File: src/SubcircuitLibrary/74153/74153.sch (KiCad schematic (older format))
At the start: 15 parts, among them U1 PORT, U2 d_inverter, U3 d_inverter, U34 d_inverter, U35 d_inverter, X1 4_OR, X10 4_and, X2 4_OR, X3 4_and, X4 4_and, X5 4_and, X6 4_and, X7 4_and, X8 4_and, X9 4_and

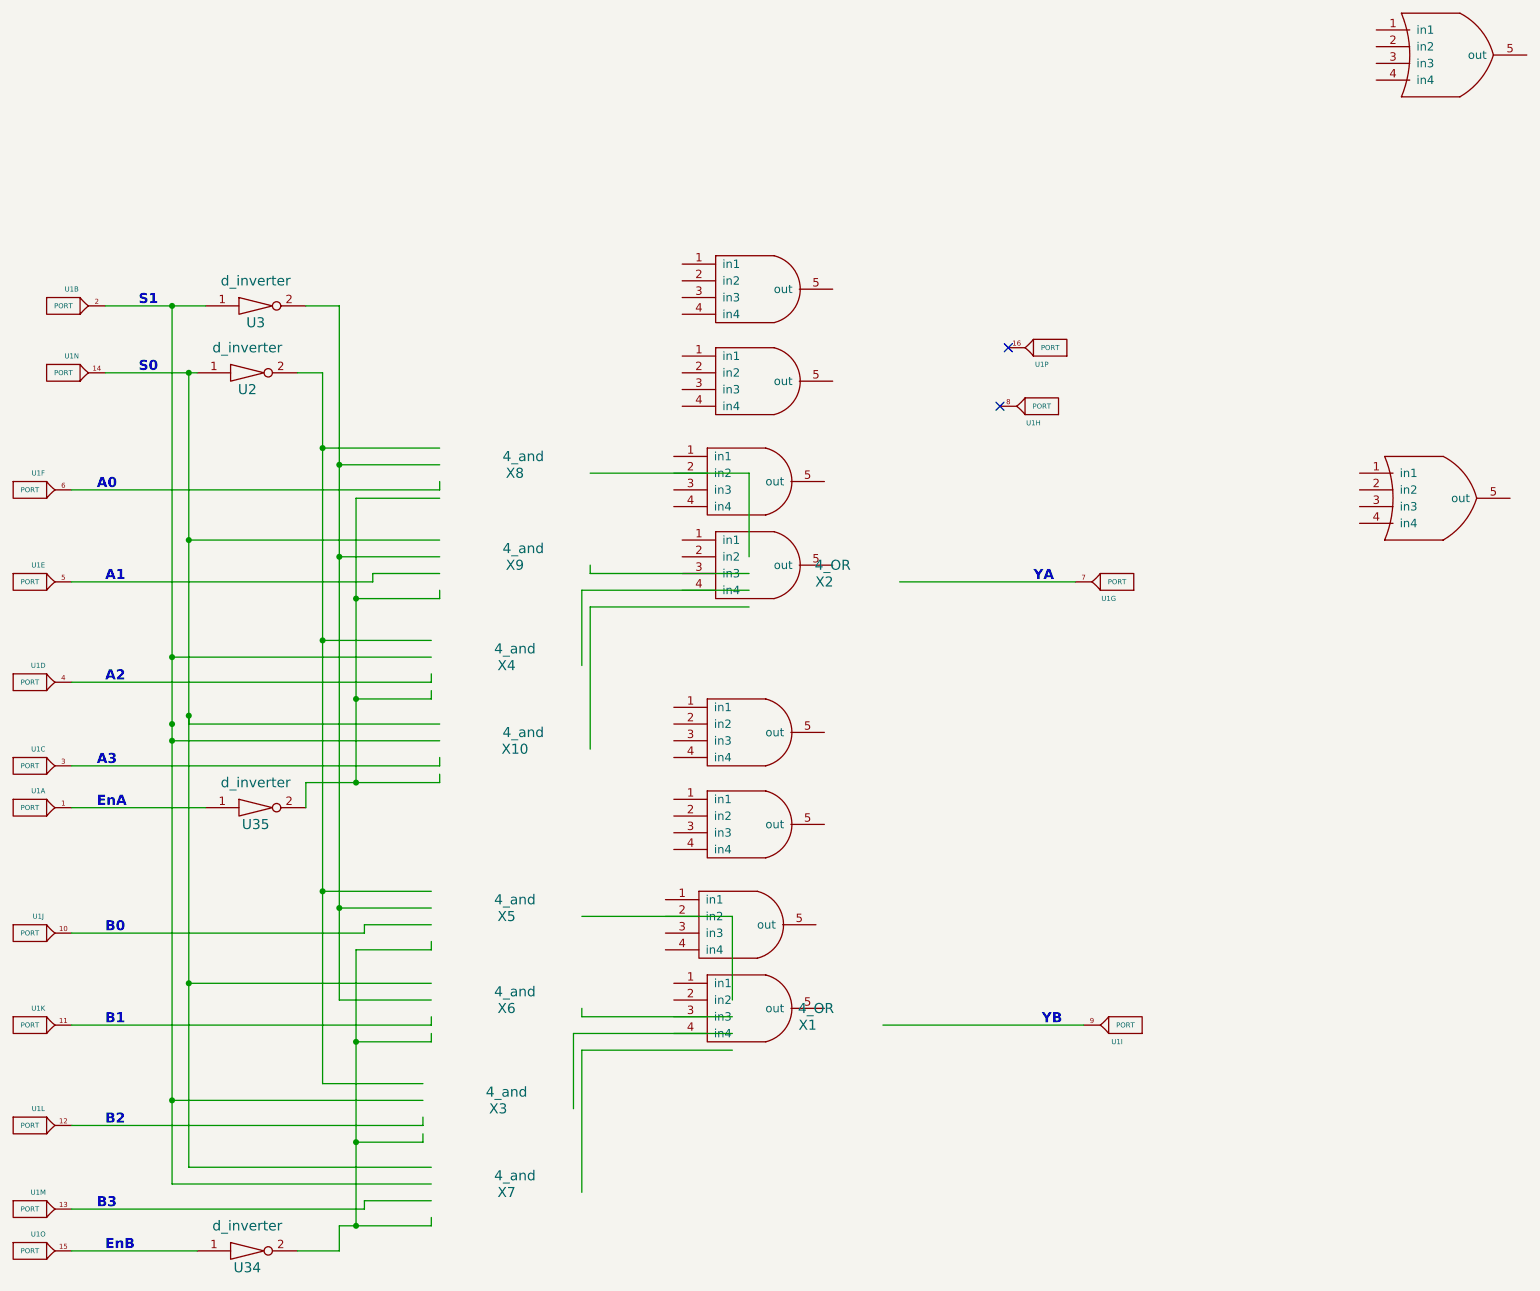
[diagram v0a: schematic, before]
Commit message: common code for Win and Linux, merged py2 changes
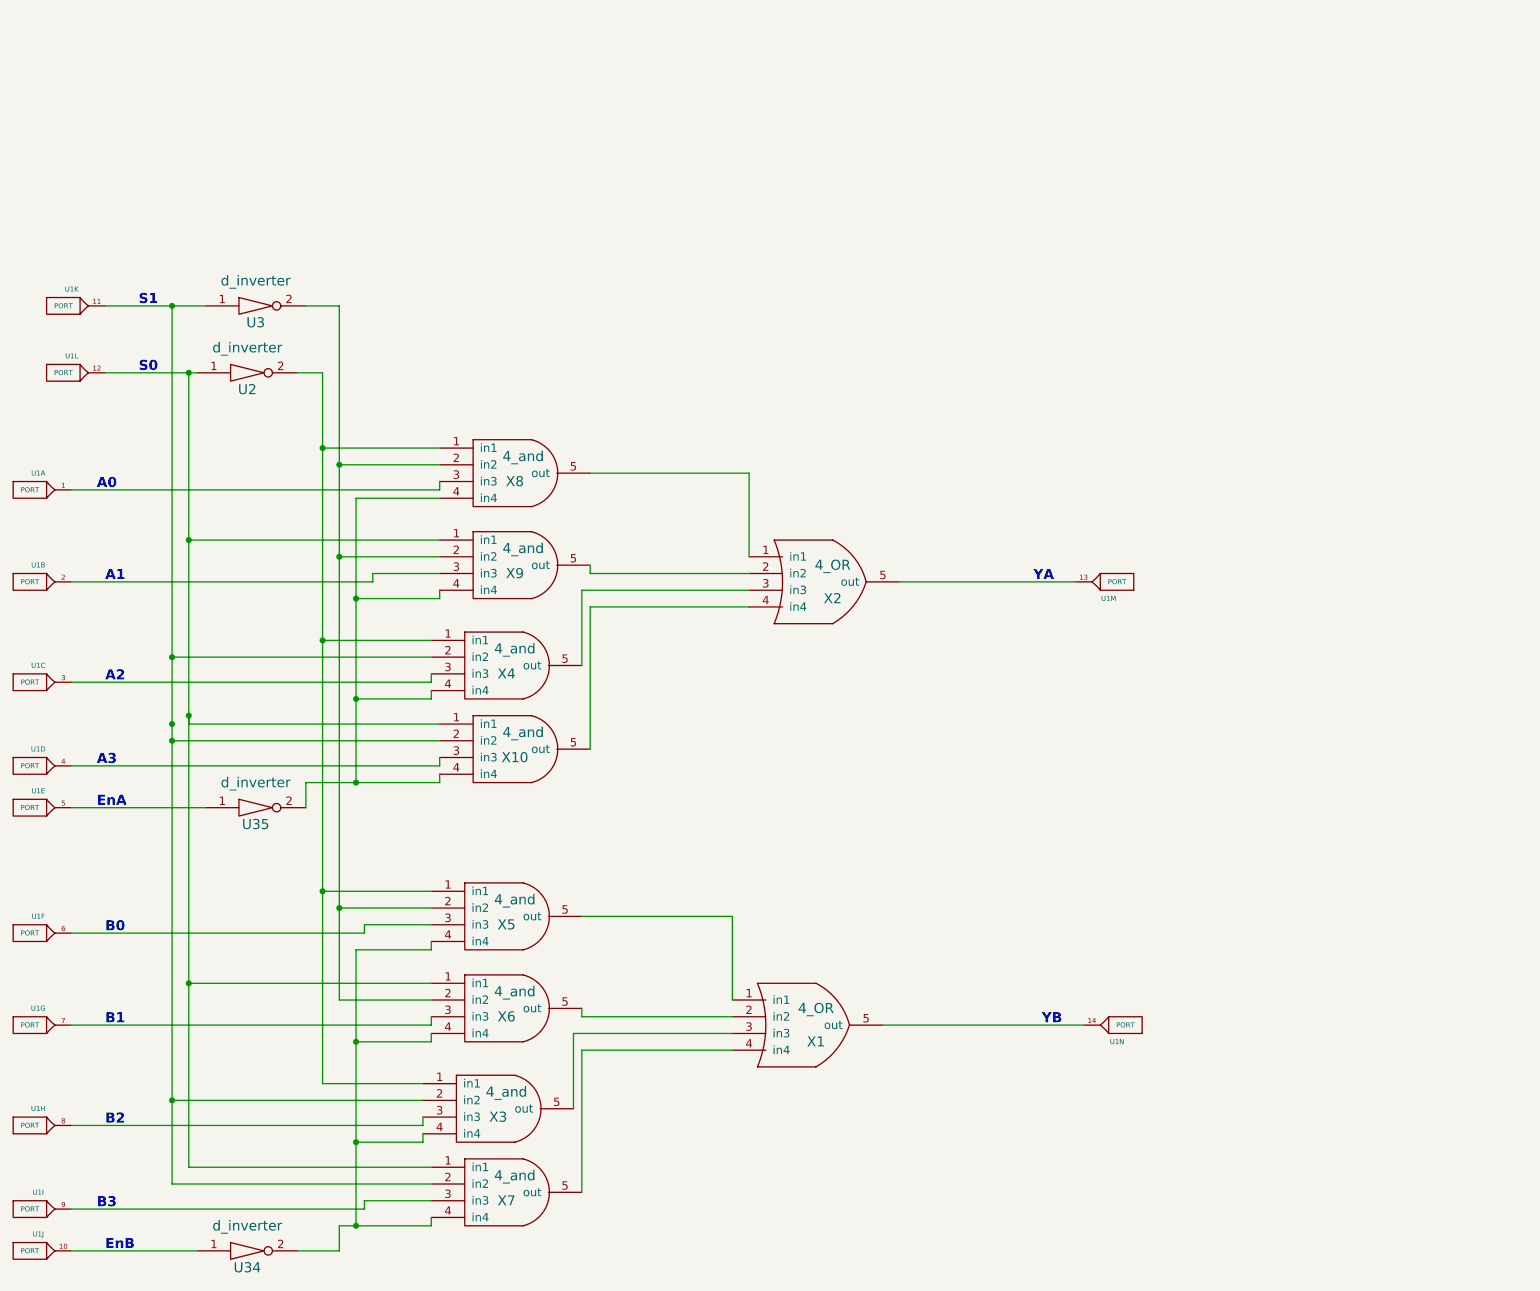
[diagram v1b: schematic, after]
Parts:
- removed unit 16 of U1
- removed unit 8 of U1
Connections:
- no-connect marks 2 -> 0
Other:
- moved on the sheet: X1, X10, X2, X3, X4, X5, X6, X7, X8, X9
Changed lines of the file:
@@
 EESchema Schematic File Version 2
+LIBS:power
+LIBS:device
+LIBS:texas
+LIBS:intel
+LIBS:audio
+LIBS:interface
+LIBS:digital-audio
+LIBS:philips
+LIBS:display
+LIBS:cypress
+LIBS:siliconi
+LIBS:opto
+LIBS:atmel
+LIBS:contrib
+LIBS:valves
 LIBS:eSim_Analog
 LIBS:eSim_Devices
@@
 LIBS:eSim_Plot
 LIBS:eSim_Power
+LIBS:eSim_PSpice
 LIBS:eSim_Sources
+LIBS:eSim_User
 LIBS:eSim_Subckt
-LIBS:eSim_User
 LIBS:74153-cache
 EELAYER 25 0
@@
 $Comp
 L PORT U1
-U 6 1 5C93A0F9
+U 1 1 5C93A0F9
 P 1350 2050
 F 0 "U1" H 1400 2150 30  0000 C CNN
@@
 F 2 "" H 1350 2050 60  0000 C CNN
 F 3 "" H 1350 2050 60  0000 C CNN
-	6    1350 2050
-	1    0    0    -1
-$EndComp
-$Comp
-L PORT U1
-U 10 1 5C93A174
+	1    1350 2050
+	1    0    0    -1
+$EndComp
+$Comp
+L PORT U1
+U 6 1 5C93A174
 P 1350 4700
 F 0 "U1" H 1400 4800 30  0000 C CNN
@@
 F 2 "" H 1350 4700 60  0000 C CNN
 F 3 "" H 1350 4700 60  0000 C CNN
-	10   1350 4700
-	1    0    0    -1
-$EndComp
-$Comp
-L PORT U1
-U 5 1 5C93AA3C
+	6    1350 4700
+	1    0    0    -1
+$EndComp
+$Comp
+L PORT U1
+U 2 1 5C93AA3C
 P 1350 2600
 F 0 "U1" H 1400 2700 30  0000 C CNN
@@
 F 2 "" H 1350 2600 60  0000 C CNN
 F 3 "" H 1350 2600 60  0000 C CNN
-	5    1350 2600
-	1    0    0    -1
-$EndComp
-$Comp
-L PORT U1
-U 4 1 5C93AACB
+	2    1350 2600
+	1    0    0    -1
+$EndComp
+$Comp
+L PORT U1
+U 3 1 5C93AACB
 P 1350 3200
 F 0 "U1" H 1400 3300 30  0000 C CNN
@@
 F 2 "" H 1350 3200 60  0000 C CNN
 F 3 "" H 1350 3200 60  0000 C CNN
-	4    1350 3200
-	1    0    0    -1
-$EndComp
-$Comp
-L PORT U1
-U 3 1 5C93AB5F
+	3    1350 3200
+	1    0    0    -1
+$EndComp
+$Comp
+L PORT U1
+U 4 1 5C93AB5F
 P 1350 3700
 F 0 "U1" H 1400 3800 30  0000 C CNN
@@
 F 2 "" H 1350 3700 60  0000 C CNN
 F 3 "" H 1350 3700 60  0000 C CNN
-	3    1350 3700
-	1    0    0    -1
-$EndComp
-$Comp
-L PORT U1
-U 11 1 5C93AD97
+	4    1350 3700
+	1    0    0    -1
+$EndComp
+$Comp
+L PORT U1
+U 7 1 5C93AD97
 P 1350 5250
 F 0 "U1" H 1400 5350 30  0000 C CNN
@@
 F 2 "" H 1350 5250 60  0000 C CNN
 F 3 "" H 1350 5250 60  0000 C CNN
-	11   1350 5250
-	1    0    0    -1
-$EndComp
-$Comp
-L PORT U1
-U 12 1 5C93ADFC
+	7    1350 5250
+	1    0    0    -1
+$EndComp
+$Comp
+L PORT U1
+U 8 1 5C93ADFC
 P 1350 5850
 F 0 "U1" H 1400 5950 30  0000 C CNN
@@
 F 2 "" H 1350 5850 60  0000 C CNN
 F 3 "" H 1350 5850 60  0000 C CNN
-	12   1350 5850
-	1    0    0    -1
-$EndComp
-$Comp
-L PORT U1
-U 13 1 5C93AE63
+	8    1350 5850
+	1    0    0    -1
+$EndComp
+$Comp
+L PORT U1
+U 9 1 5C93AE63
 P 1350 6350
 F 0 "U1" H 1400 6450 30  0000 C CNN
@@
 F 2 "" H 1350 6350 60  0000 C CNN
 F 3 "" H 1350 6350 60  0000 C CNN
-	13   1350 6350
-	1    0    0    -1
-$EndComp
-$Comp
-L PORT U1
-U 1 1 5C93AECA
+	9    1350 6350
+	1    0    0    -1
+$EndComp
+$Comp
+L PORT U1
+U 5 1 5C93AECA
 P 1350 3950
 F 0 "U1" H 1400 4050 30  0000 C CNN
@@
 F 2 "" H 1350 3950 60  0000 C CNN
 F 3 "" H 1350 3950 60  0000 C CNN
-	1    1350 3950
-	1    0    0    -1
-$EndComp
-$Comp
-L PORT U1
-U 15 1 5C93AF79
+	5    1350 3950
+	1    0    0    -1
+$EndComp
+$Comp
+L PORT U1
+U 10 1 5C93AF79
 P 1350 6600
 F 0 "U1" H 1400 6700 30  0000 C CNN
@@
 F 2 "" H 1350 6600 60  0000 C CNN
 F 3 "" H 1350 6600 60  0000 C CNN
-	15   1350 6600
-	1    0    0    -1
-$EndComp
-$Comp
-L PORT U1
-U 2 1 5C93B10A
+	10   1350 6600
+	1    0    0    -1
+$EndComp
+$Comp
+L PORT U1
+U 11 1 5C93B10A
 P 1550 950
 F 0 "U1" H 1600 1050 30  0000 C CNN
@@
 F 2 "" H 1550 950 60  0000 C CNN
 F 3 "" H 1550 950 60  0000 C CNN
-	2    1550 950
-	1    0    0    -1
-$EndComp
-$Comp
-L PORT U1
-U 14 1 5C93B179
+	11   1550 950
+	1    0    0    -1
+$EndComp
+$Comp
+L PORT U1
+U 12 1 5C93B179
 P 1550 1350
 F 0 "U1" H 1600 1450 30  0000 C CNN
@@
 F 2 "" H 1550 1350 60  0000 C CNN
 F 3 "" H 1550 1350 60  0000 C CNN
-	14   1550 1350
-	1    0    0    -1
-$EndComp
-$Comp
-L PORT U1
-U 7 1 5C93B567
+	12   1550 1350
+	1    0    0    -1
+$EndComp
+$Comp
+L PORT U1
+U 13 1 5C93B567
 P 7850 2600
 F 0 "U1" H 7900 2700 30  0000 C CNN
@@
 F 2 "" H 7850 2600 60  0000 C CNN
 F 3 "" H 7850 2600 60  0000 C CNN
-	7    7850 2600
+	13   7850 2600
 	-1   0    0    1
 $EndComp
 $Comp
 L PORT U1
-U 9 1 5C93B5DA
+U 14 1 5C93B5DA
 P 7900 5250
 F 0 "U1" H 7950 5350 30  0000 C CNN
@@
 F 2 "" H 7900 5250 60  0000 C CNN
 F 3 "" H 7900 5250 60  0000 C CNN
-	9    7900 5250
+	14   7900 5250
 	-1   0    0    1
 $EndComp
@@
 L 4_and X8
 U 1 1 5C9D0C22
-P 4200 1950
-F 0 "X8" H 4250 1950 60  0000 C CNN
-F 1 "4_and" H 4300 2050 60  0000 C CNN
-F 2 "" H 4200 1950 60  0000 C CNN
-F 3 "" H 4200 1950 60  0000 C CNN
-	1    4200 1950
+P 2750 3050
+F 0 "X8" H 4250 4100 60  0000 C CNN
+F 1 "4_and" H 4300 4250 60  0000 C CNN
+F 2 "" H 2750 3050 60  0000 C CNN
+F 3 "" H 2750 3050 60  0000 C CNN
+	1    2750 3050
 	1    0    0    -1
 $EndComp
@@
 L 4_and X9
 U 1 1 5C9D0CA2
-P 4200 2500
-F 0 "X9" H 4250 2500 60  0000 C CNN
-F 1 "4_and" H 4300 2600 60  0000 C CNN
-F 2 "" H 4200 2500 60  0000 C CNN
-F 3 "" H 4200 2500 60  0000 C CNN
-	1    4200 2500
+P 2750 3600
+F 0 "X9" H 4250 4650 60  0000 C CNN
+F 1 "4_and" H 4300 4800 60  0000 C CNN
+F 2 "" H 2750 3600 60  0000 C CNN
+F 3 "" H 2750 3600 60  0000 C CNN
+	1    2750 3600
 	1    0    0    -1
 $EndComp
@@
 L 4_and X4
 U 1 1 5C9D0D16
-P 4150 3100
-F 0 "X4" H 4200 3100 60  0000 C CNN
-F 1 "4_and" H 4250 3200 60  0000 C CNN
-F 2 "" H 4150 3100 60  0000 C CNN
-F 3 "" H 4150 3100 60  0000 C CNN
-	1    4150 3100
+P 2700 4200
+F 0 "X4" H 4200 5250 60  0000 C CNN
+F 1 "4_and" H 4250 5400 60  0000 C CNN
+F 2 "" H 2700 4200 60  0000 C CNN
+F 3 "" H 2700 4200 60  0000 C CNN
+	1    2700 4200
 	1    0    0    -1
 $EndComp
@@
 L 4_and X10
 U 1 1 5C9D0D93
-P 4200 3600
-F 0 "X10" H 4250 3600 60  0000 C CNN
-F 1 "4_and" H 4300 3700 60  0000 C CNN
-F 2 "" H 4200 3600 60  0000 C CNN
-F 3 "" H 4200 3600 60  0000 C CNN
-	1    4200 3600
+P 2750 4700
+F 0 "X10" H 4250 5750 60  0000 C CNN
+F 1 "4_and" H 4300 5900 60  0000 C CNN
+F 2 "" H 2750 4700 60  0000 C CNN
+F 3 "" H 2750 4700 60  0000 C CNN
+	1    2750 4700
 	1    0    0    -1
 $EndComp
@@
 L 4_and X5
 U 1 1 5C9D182A
-P 4150 4600
-F 0 "X5" H 4200 4600 60  0000 C CNN
-F 1 "4_and" H 4250 4700 60  0000 C CNN
-F 2 "" H 4150 4600 60  0000 C CNN
-F 3 "" H 4150 4600 60  0000 C CNN
-	1    4150 4600
+P 2700 5700
+F 0 "X5" H 4200 6750 60  0000 C CNN
+F 1 "4_and" H 4250 6900 60  0000 C CNN
+F 2 "" H 2700 5700 60  0000 C CNN
+F 3 "" H 2700 5700 60  0000 C CNN
+	1    2700 5700
 	1    0    0    -1
 $EndComp
@@
 L 4_and X6
 U 1 1 5C9D1830
-P 4150 5150
-F 0 "X6" H 4200 5150 60  0000 C CNN
-F 1 "4_and" H 4250 5250 60  0000 C CNN
-F 2 "" H 4150 5150 60  0000 C CNN
-F 3 "" H 4150 5150 60  0000 C CNN
-	1    4150 5150
+P 2700 6250
+F 0 "X6" H 4200 7300 60  0000 C CNN
+F 1 "4_and" H 4250 7450 60  0000 C CNN
+F 2 "" H 2700 6250 60  0000 C CNN
+F 3 "" H 2700 6250 60  0000 C CNN
+	1    2700 6250
 	1    0    0    -1
 $EndComp
@@
 L 4_and X3
 U 1 1 5C9D1836
-P 4100 5750
-F 0 "X3" H 4150 5750 60  0000 C CNN
-F 1 "4_and" H 4200 5850 60  0000 C CNN
-F 2 "" H 4100 5750 60  0000 C CNN
-F 3 "" H 4100 5750 60  0000 C CNN
-	1    4100 5750
+P 2650 6850
+F 0 "X3" H 4150 7900 60  0000 C CNN
+F 1 "4_and" H 4200 8050 60  0000 C CNN
+F 2 "" H 2650 6850 60  0000 C CNN
+F 3 "" H 2650 6850 60  0000 C CNN
+	1    2650 6850
 	1    0    0    -1
 $EndComp
@@
 L 4_and X7
 U 1 1 5C9D183C
-P 4150 6250
-F 0 "X7" H 4200 6250 60  0000 C CNN
-F 1 "4_and" H 4250 6350 60  0000 C CNN
-F 2 "" H 4150 6250 60  0000 C CNN
-F 3 "" H 4150 6250 60  0000 C CNN
-	1    4150 6250
+P 2700 7350
+F 0 "X7" H 4200 8400 60  0000 C CNN
+F 1 "4_and" H 4250 8550 60  0000 C CNN
+F 2 "" H 2700 7350 60  0000 C CNN
+F 3 "" H 2700 7350 60  0000 C CNN
+	1    2700 7350
 	1    0    0    -1
 $EndComp
@@
 L 4_OR X1
 U 1 1 5C9D22F7
-P 5900 5250
-F 0 "X1" H 6000 5250 60  0000 C CNN
-F 1 "4_OR" H 6050 5350 60  0000 C CNN
-F 2 "" H 5900 5250 60  0000 C CNN
-F 3 "" H 5900 5250 60  0000 C CNN
-	1    5900 5250
+P 2150 8400
+F 0 "X1" H 6050 11450 60  0000 C CNN
+F 1 "4_OR" H 6050 11650 60  0000 C CNN
+F 2 "" H 2150 8400 60  0000 C CNN
+F 3 "" H 2150 8400 60  0000 C CNN
+	1    2150 8400
 	1    0    0    -1
 $EndComp
@@
 L 4_OR X2
 U 1 1 5C9D28DE
-P 6000 2600
-F 0 "X2" H 6100 2600 60  0000 C CNN
-F 1 "4_OR" H 6150 2700 60  0000 C CNN
-F 2 "" H 6000 2600 60  0000 C CNN
-F 3 "" H 6000 2600 60  0000 C CNN
-	1    6000 2600
+P 2250 5750
+F 0 "X2" H 6150 8800 60  0000 C CNN
+F 1 "4_OR" H 6150 9000 60  0000 C CNN
+F 2 "" H 2250 5750 60  0000 C CNN
+F 3 "" H 2250 5750 60  0000 C CNN
+	1    2250 5750
 	1    0    0    -1
 $EndComp
@@
 Wire Wire Line
 	4700 2750 5650 2750
-$Comp
-L PORT U1
-U 16 1 5D11F8AE
-P 7450 1200
-F 0 "U1" H 7500 1300 30  0000 C CNN
-F 1 "PORT" H 7450 1200 30  0000 C CNN
-F 2 "" H 7450 1200 60  0000 C CNN
-F 3 "" H 7450 1200 60  0000 C CNN
-	16   7450 1200
-	-1   0    0    1
-$EndComp
-$Comp
-L PORT U1
-U 8 1 5D11F97A
-P 7400 1550
-F 0 "U1" H 7450 1650 30  0000 C CNN
-F 1 "PORT" H 7400 1550 30  0000 C CNN
-F 2 "" H 7400 1550 60  0000 C CNN
-F 3 "" H 7400 1550 60  0000 C CNN
-	8    7400 1550
-	-1   0    0    1
-$EndComp
-NoConn ~ 7200 1200
-NoConn ~ 7150 1550
 $EndSCHEMATC
